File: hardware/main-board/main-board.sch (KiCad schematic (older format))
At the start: 30 parts, among them J2 STDC14, J3 NHD OLED Connector, U4 STM32F411RETx, U5 PAM8904EJP, U6 M24M01-RMN, Y1 16MHz

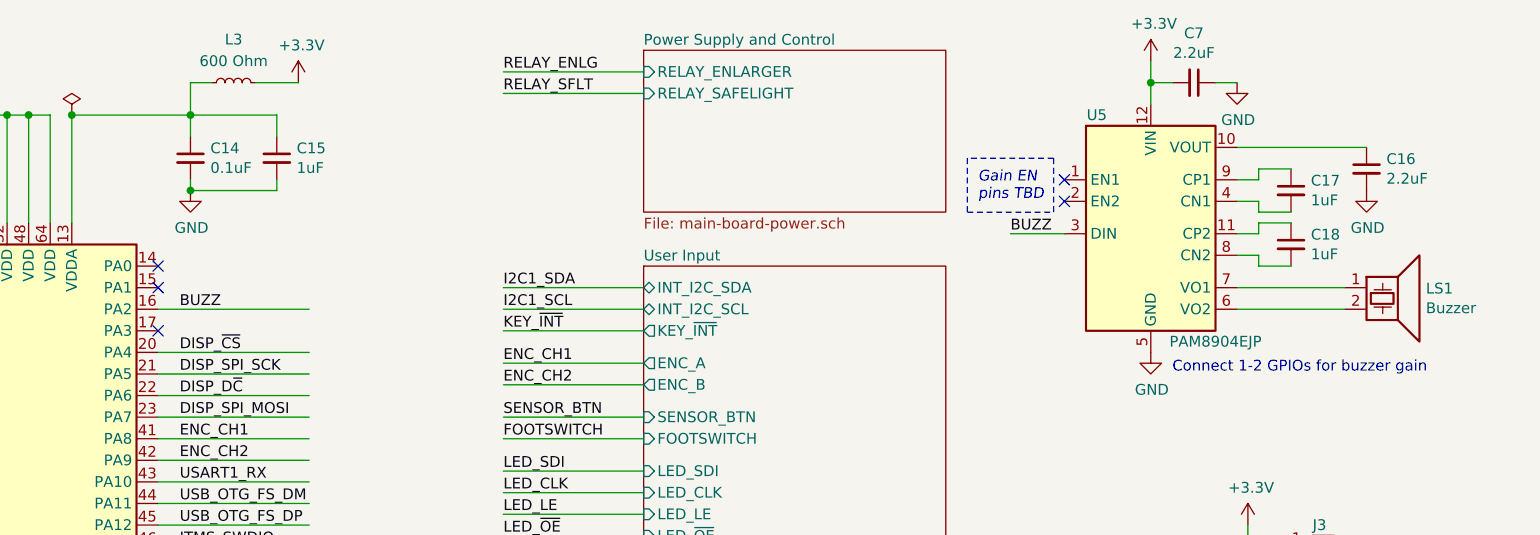
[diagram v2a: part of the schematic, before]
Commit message: Added gain control for the piezo driver
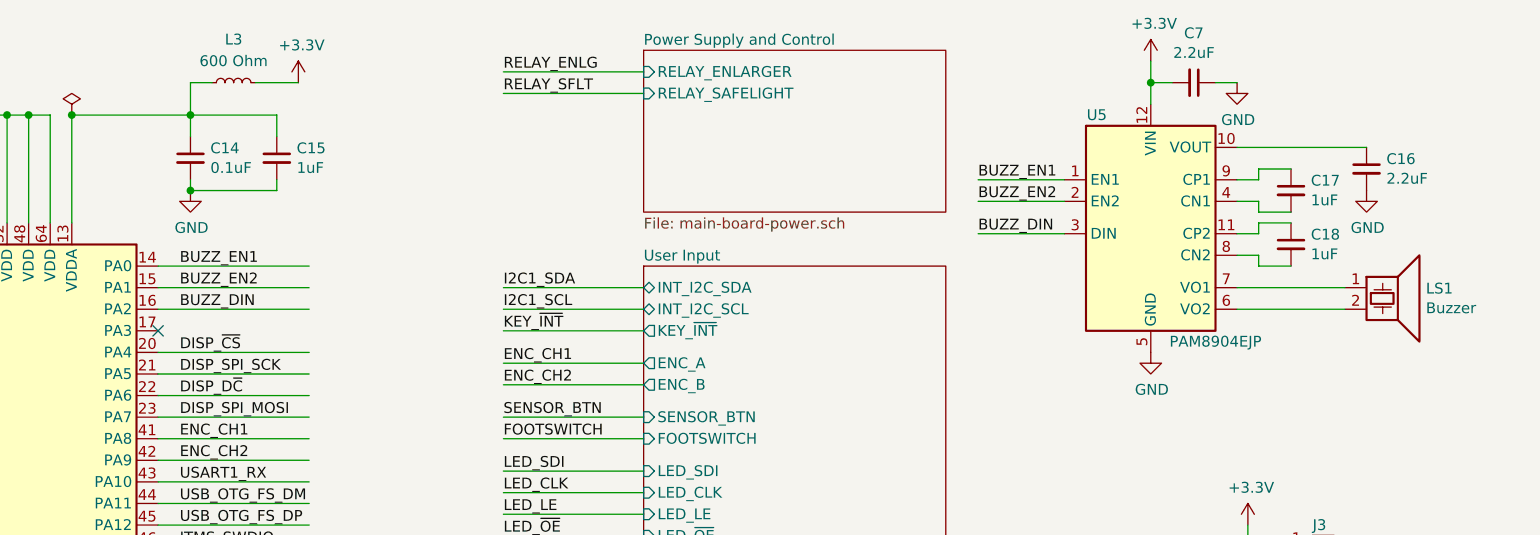
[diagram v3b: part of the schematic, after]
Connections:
- net labels added: BUZZ_DIN, BUZZ_EN1, BUZZ_EN2
- net labels removed: BUZZ
- wire segments 202 -> 206
- no-connect marks 30 -> 26
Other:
- note removed: "Connect 1-2 GPIOs for buzzer gain"
- note removed: "Gain EN\npins TBD"
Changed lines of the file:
@@
 RESET
 Text Label 4400 1950 0    50   ~ 0
-BUZZ
+BUZZ_DIN
 Wire Wire Line
 	4300 1950 5000 1950
@@
 	1    0    0    -1
 $EndComp
-Text Label 8250 1600 0    50   ~ 0
-BUZZ
-Wire Wire Line
-	8500 1600 8250 1600
-Text Notes 9000 2250 0    50   ~ 0
-Connect 1-2 GPIOs for buzzer gain
 Text Label 2250 4050 0    50   ~ 0
 LED_CLK
@@
 Wire Wire Line
 	6550 3000 5900 3000
-NoConn ~ 4300 1750
-NoConn ~ 4300 1850
 NoConn ~ 4300 2050
 NoConn ~ 4300 3450
@@
 NoConn ~ 2900 3350
 NoConn ~ 2900 3150
-NoConn ~ 8500 1350
-NoConn ~ 8500 1450
-Text Notes 8100 1450 0    50   Italic 0
-Gain EN\npins TBD
 $Comp
 L power:PWR_FLAG #FLG0108
@@
 $EndComp
 Connection ~ 2650 2150
-Wire Notes Line
-	8450 1500 8450 1250
-Wire Notes Line
-	8450 1250 8050 1250
-Wire Notes Line
-	8050 1250 8050 1500
-Wire Notes Line
-	8050 1500 8450 1500
 NoConn ~ 1450 7450
 Wire Wire Line
@@
 Wire Wire Line
 	5900 2300 6550 2300
+Text Label 4400 1850 0    50   ~ 0
+BUZZ_EN2
+Text Label 4400 1750 0    50   ~ 0
+BUZZ_EN1
+Wire Wire Line
+	4300 1850 5000 1850
+Wire Wire Line
+	4300 1750 5000 1750
+Text Label 8100 1600 0    50   ~ 0
+BUZZ_DIN
+Text Label 8100 1350 0    50   ~ 0
+BUZZ_EN1
+Text Label 8100 1450 0    50   ~ 0
+BUZZ_EN2
+Wire Wire Line
+	8500 1350 8100 1350
+Wire Wire Line
+	8500 1450 8100 1450
+Wire Wire Line
+	8500 1600 8100 1600
 $EndSCHEMATC

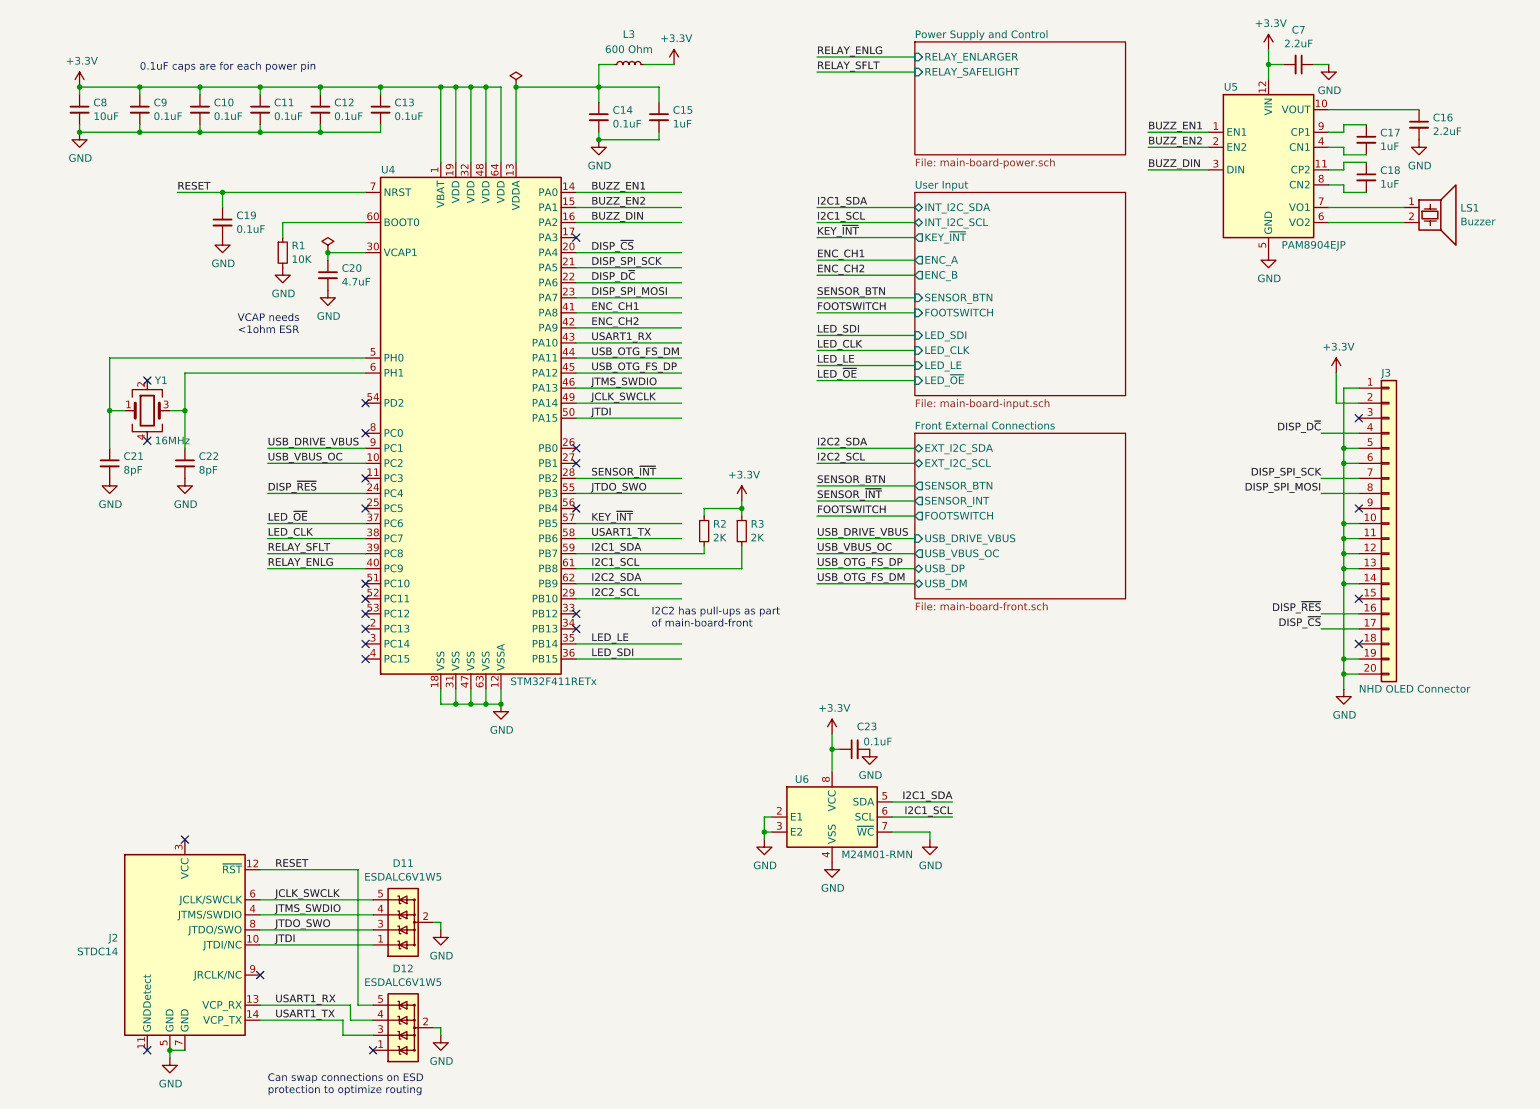
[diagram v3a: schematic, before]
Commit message: Main board schematic cleanup pass
Added mounting holes for the board and the OLED module
Connected GND and Earth nets
Cleaned up and labeled many parts of the schematic
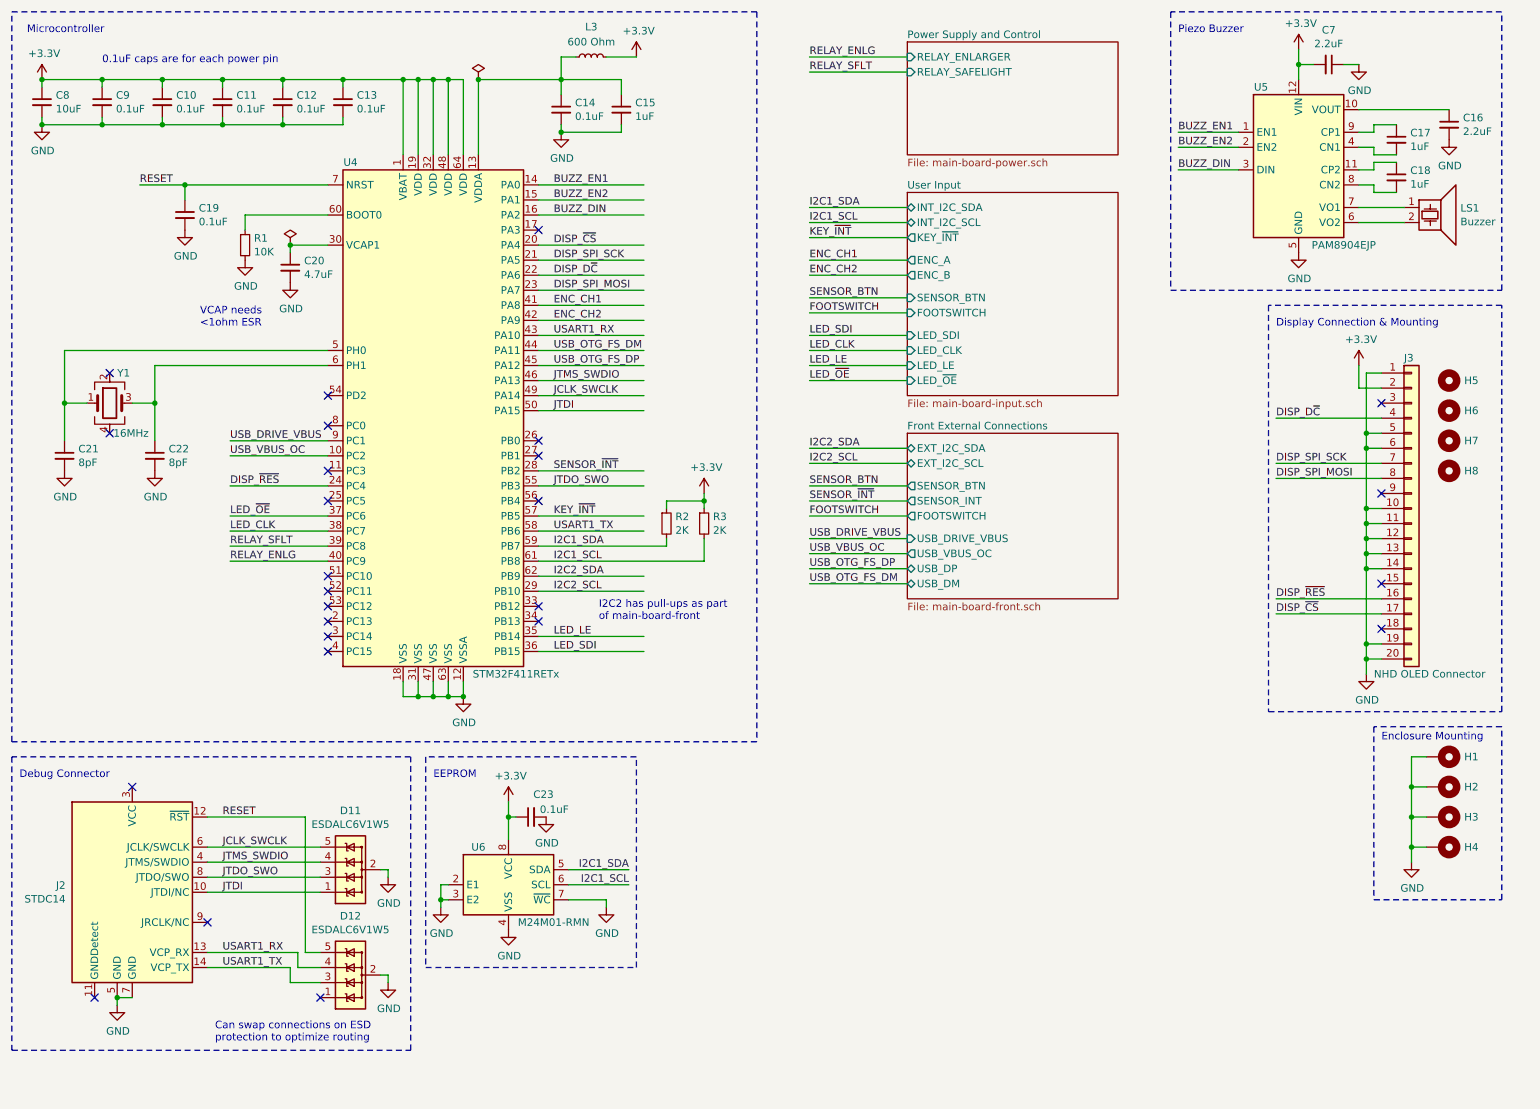
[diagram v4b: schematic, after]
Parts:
- added H1, H2, H3, H4: MountingHole_Pad, MountingHole:MountingHole_3.2mm_M3_Pad_Via, symbol Mechanical:MountingHole_Pad
- added H5, H6, H7, H8: MountingHole, MountingHole:MountingHole_2.7mm_M2.5_Pad, symbol Mechanical:MountingHole
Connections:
- wire segments 206 -> 214
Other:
- note added: "Debug Connector"
- note added: "Display Connection & Mounting"
- note added: "EEPROM"
- note added: "Enclosure Mounting"
- note added: "Microcontroller"
- note added: "Piezo Buzzer"
- moved on the sheet: C10, C11, C12, C13, C14, C15, C16, C17, C18, C19, C20, C21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
